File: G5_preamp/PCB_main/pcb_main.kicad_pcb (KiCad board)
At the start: 2 copper layers, 165 x 58 mm, 47 parts, among them J1 PSU_TUBE, J2 PCB_TUBE, J3 PSU_AMP, J4 AMP, J5 PSU_SIMCAB, J6 SIMCAB, J8 LEVEL 3-2, SW1 Boost, SW2 SIMCAB

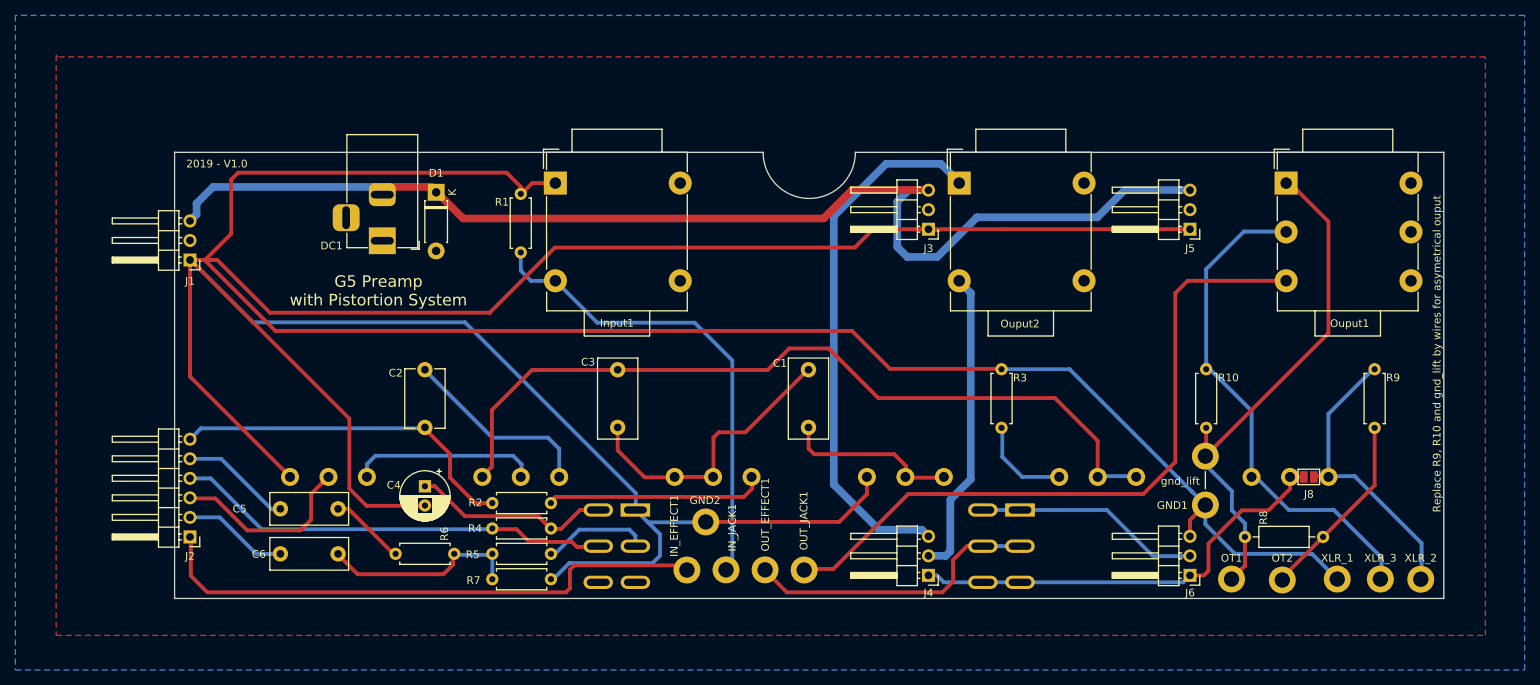
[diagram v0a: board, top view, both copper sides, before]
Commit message: DC-DC move
DC-DC Converter move from PCB_tube to PCB_main
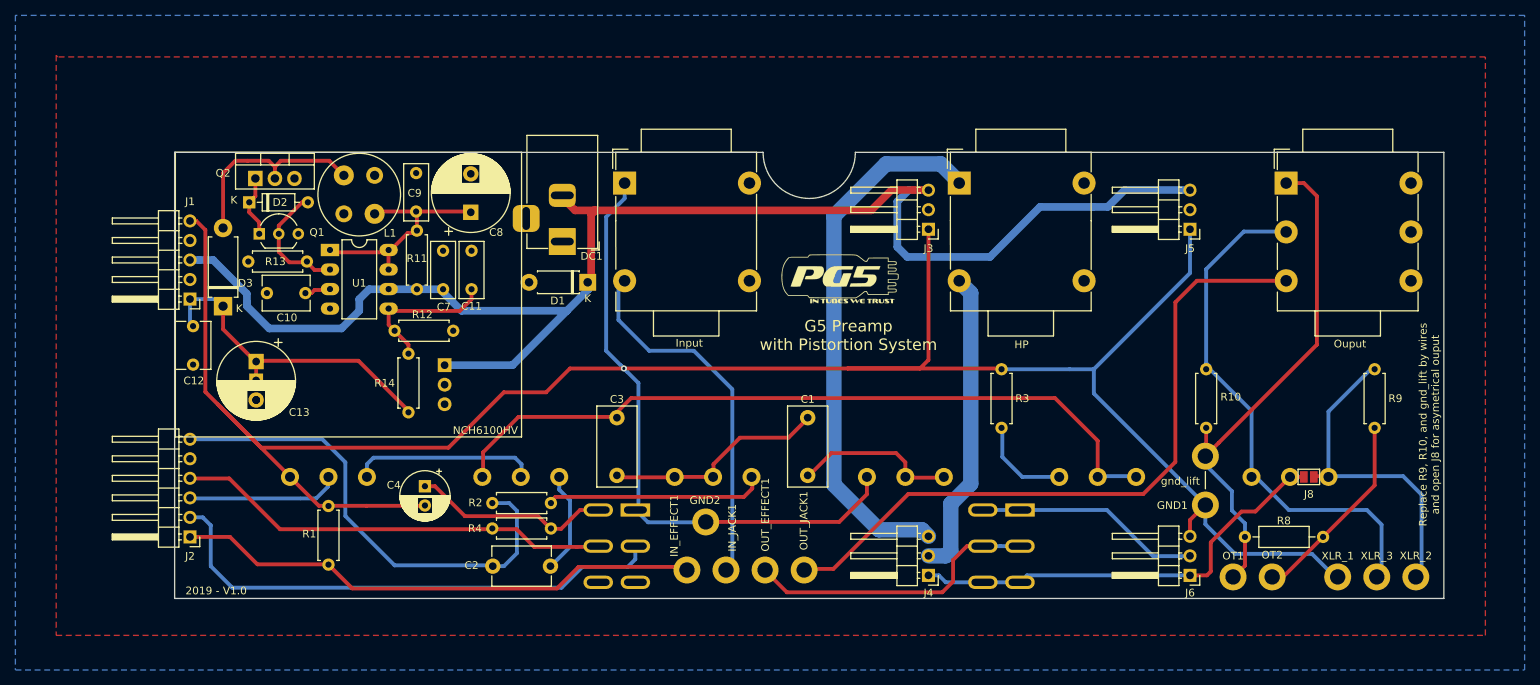
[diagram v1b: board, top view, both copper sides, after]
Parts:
- removed C5, C6: 22nF, Capacitor_THT:C_Rect_L10.0mm_W4.0mm_P7.50mm_MKS4
- removed Input1: Input, ProjectLib_main:Jack_6.35mm_Neutrik_NMJ4HCD2_Horizontal
- removed Ouput2: HP, ProjectLib_main:Jack_6.35mm_Neutrik_NMJ4HCD2_Horizontal
- removed R5: 100k, Resistor_THT:R_Axial_DIN0207_L6.3mm_D2.5mm_P7.62mm_Horizontal
- removed R6, R7: 470k, Resistor_THT:R_Axial_DIN0207_L6.3mm_D2.5mm_P7.62mm_Horizontal
- added C10: 470p, Capacitor_THT:C_Disc_D6.0mm_W4.4mm_P5.00mm, F.Cu at (97.0, 120.3)
- added C11: 100n, Capacitor_THT:C_Rect_L7.2mm_W3.0mm_P5.00mm_FKS2_FKP2_MKS2_MKP2, F.Cu at (118.6, 119.8)
- added C12: 10n/400V, Capacitor_THT:C_Disc_D6.0mm_W4.4mm_P5.00mm, F.Cu at (82.4, 124.6)
- added C13: 4.7µ/350V, Capacitor_THT:CP_Radial_D10.0mm_P5.00mm, F.Cu at (90.6, 129.2)
- added C7: 100n, Capacitor_THT:C_Rect_L7.2mm_W3.0mm_P5.00mm_FKS2_FKP2_MKS2_MKP2, F.Cu at (114.9, 119.8)
- added C8: 470µ, Capacitor_THT:CP_Radial_D10.0mm_P5.00mm, F.Cu at (118.5, 109.8)
- added C9: 100n, Capacitor_THT:C_Rect_L7.2mm_W3.0mm_P5.00mm_FKS2_FKP2_MKS2_MKP2, F.Cu at (111.4, 109.7)
- added D2: 1N4148, Diode_THT:D_DO-35_SOD27_P7.62mm_Horizontal, F.Cu at (89.7, 108.5)
- added D3: BYV26, Diode_THT:D_DO-15_P10.16mm_Horizontal, F.Cu at (86.3, 122.0)
- added HP: HP, ProjectLib_main:Jack_6.35mm_Neutrik_NMJ4HCD2_Horizontal, F.Cu at (182.0, 118.7)
- added Input: Input, ProjectLib_main:Jack_6.35mm_Neutrik_NMJ4HCD2_Horizontal, F.Cu at (138.5, 118.7)
- added L1: 220µH/1.5A, ProjectLib_main:L_Radial_D10.5mm_P5.00mm_MuRATA_1200RS, F.Cu at (106.0, 110.0)
- added NCH6100HV: NCH6100HV, Converter_DCDC:NCH6100HV, F.Cu at (125.1, 139.0)
- added Q1: MPS751, Package_TO_SOT_THT:TO-92_Inline_Wide, F.Cu at (91.0, 112.6)
- added Q2: IRF740, Package_TO_SOT_THT:TO-220-3_Vertical, F.Cu at (90.5, 105.4)
- added R11: 0.22R, Resistor_THT:R_Axial_DIN0207_L6.3mm_D2.5mm_P7.62mm_Horizontal, F.Cu at (111.5, 119.8)
- added R12: 1.8k, Resistor_THT:R_Axial_DIN0207_L6.3mm_D2.5mm_P7.62mm_Horizontal, F.Cu at (108.6, 125.2)
- added R13: 1k, Resistor_THT:R_Axial_DIN0207_L6.3mm_D2.5mm_P7.62mm_Horizontal, F.Cu at (97.2, 116.2)
- added R14: 430k, Resistor_THT:R_Axial_DIN0207_L6.3mm_D2.5mm_P7.62mm_Horizontal, F.Cu at (110.4, 135.8)
- added REF**: PG5_Logo_15mm_SilkScreen, Symbol:PG5_Logo_15mm_SilkScreen, F.Cu at (166.5, 118.2)
- added U1: MC34063AP, Package_DIP:DIP-8_W7.62mm_LongPads, F.Cu at (100.2, 114.7)
- J1: footprint Connector_PinHeader_2.54mm:PinHeader_1x03_P2.54mm_Horizontal -> Connector_PinHeader_2.54mm:PinHeader_1x05_P2.54mm_Horizontal
- SW1, SW2: footprint ProjectLib_main:SW_CK_Lever_DPDT_72xx -> Switch_lever:SW_CK_Lever_DPDT_72xx
- moved R1 47.7 mm to (100.0, 155.6)
- moved C2 30.3 mm to (128.9, 155.8), turned to 180 degrees
- moved DC1 23.4 mm to (130.4, 113.6)
- moved D1 22.9 mm to (133.7, 118.9), turned to 180 degrees
- moved C1 6.24 mm to (162.3, 136.5)
- moved C3 6.24 mm to (137.5, 136.5)
- moved J1 5.08 mm to (82.0, 121.1)
- moved OT2 1.38 mm to (222.7, 157.2)
- moved XLR_2 0.71 mm to (241.4, 157.2)
- moved XLR_3 0.55 mm to (236.3, 157.2)
- moved OT1 0.34 mm to (217.6, 157.2)
- moved XLR_1 0.29 mm to (231.2, 157.2)
- renumbered Ouput1 to Ouput
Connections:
- net /SIMCAB_IN renamed /LINE_OUT
- D1 pad 2: GND -> GNDREF
- DC1 pad 1: GND -> GNDREF
- J1 pad 1: GNDS -> /HT2
- J1 pad 2: GND -> Net-(J1-Pad2)
- J2 pad 2: /G_V2 -> /BOOST
- J2 pad 5: /A_V1B -> Net-(J2-Pad5)
- J3 pad 2: GND -> GNDREF
- J4 pad 2: Net-(J4-Pad2) -> /HP1
- J4 pad 3: Net-(J4-Pad3) -> /HP2
- J5 pad 2: GND -> GNDREF
- R1 pad 1: Net-(IN_JACK1-Pad1) -> /IN_EFFECT
- SW1 pad 2: Net-(R5-Pad2) -> /BOOST
- SW1 pad 3: (no net) -> Net-(SW1-Pad3)
- SW1 pad 6: (no net) -> Net-(SW1-Pad6)
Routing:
- net GNDS: track 580.3 -> 360.9 mm, vias 0 -> 1
- net Net-(J4-Pad3): track 70.0 -> 0.00 mm
- net /HP2: track 0.00 -> 70.0 mm
- net /BOOST: track 0.00 -> 68.0 mm
- net /HT2: track 0.00 -> 43.6 mm
- net /HP1: track 0.00 -> 39.9 mm
- net Net-(J4-Pad2): track 39.9 -> 0.00 mm
- net +24V: track 154.9 -> 194.4 mm
- net /PEAK: track 0.00 -> 29.7 mm
- net Net-(C6-Pad2): track 25.9 -> 0.00 mm
- net /HT1: track 0.00 -> 25.6 mm
- net Net-(C11-Pad1): track 0.00 -> 19.4 mm
- net /A_V1A: track 45.9 -> 63.2 mm
- net Net-(D2-Pad2): track 0.00 -> 16.2 mm
- net Net-(IN_JACK1-Pad1): track 62.5 -> 47.8 mm
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- added copper zone on B.Cu, net GNDREF
- added copper zone on F.Cu, net GNDREF
- removed copper zone on B.Cu, net GND
- removed copper zone on F.Cu, net GND
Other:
- board text added: "Replace R9, R10, and gnd_lift by wires and open J8 for asymetrical ouput"
- board text removed: "Replace R9, R10 and gnd_lift by wires for asymetrical ouput"

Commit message: Gerber export
Last MAJ with GERBER
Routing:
- net Net-(IN_JACK1-Pad1): track 47.8 -> 43.7 mm
- net GNDS: track 360.9 -> 362.4 mm
- net /G_V1B: track 19.8 -> 19.1 mm
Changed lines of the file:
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@@
     (thickness 1.6)
     (drawings 11)
-    (tracks 333)
+    (tracks 326)
     (zones 0)
     (modules 61)
@@
   (layers
     (0 F.Cu signal)
-    (31 B.Cu signal)
+    (31 B.Cu signal hide)
     (32 B.Adhes user)
     (33 F.Adhes user)
@@
     (visible_elements 7FFFFF7F)
     (pcbplotparams
-      (layerselection 0x010fc_ffffffff)
-      (usegerberextensions false)
+      (layerselection 0x010f0_ffffffff)
+      (usegerberextensions true)
       (usegerberattributes false)
       (usegerberadvancedattributes false)
@@
       (drillshape 0)
       (scaleselection 1)
-      (outputdirectory ""))
+      (outputdirectory "GERBER/"))
   )
   (net 0 "")
@@
   (gr_line (start 245 160) (end 245 102) (layer Edge.Cuts) (width 0.1))
   (gr_line (start 80 160) (end 245 160) (layer Edge.Cuts) (width 0.1))
-  (segment (start 212 106.9) (end 203.5 106.9) (width 1) (layer B.Cu) (net 1) (status 10))
   (segment (start 82 116) (end 81.9 116.1) (width 1) (layer F.Cu) (net 1) (status 30))
   (segment (start 82.1 116) (end 82.05 116) (width 1) (layer B.Cu) (net 1) (status 30))
@@
   (segment (start 134.449999 109.549999) (end 132.049999 109.549999) (width 1) (layer F.Cu) (net 1))
   (segment (start 132.049999 109.549999) (end 130.1 107.6) (width 1) (layer F.Cu) (net 1) (status 20))
-  (segment (start 201.3 109.1) (end 199.4 109.1) (width 1) (layer B.Cu) (net 1))
-  (segment (start 203.5 106.9) (end 201.3 109.1) (width 1) (layer B.Cu) (net 1))
-  (segment (start 175.45 106.9) (end 178.1 106.9) (width 1) (layer B.Cu) (net 1))
-  (segment (start 192.5 109.1) (end 186 115.6) (width 1) (layer B.Cu) (net 1))
-  (segment (start 199.4 109.1) (end 192.5 109.1) (width 1) (layer B.Cu) (net 1))
-  (segment (start 186 115.6) (end 175.25 115.6) (width 1) (layer B.Cu) (net 1))
-  (segment (start 175.25 115.6) (end 173.95 114.3) (width 1) (layer B.Cu) (net 1))
-  (segment (start 173.95 114.3) (end 173.95 108.4) (width 1) (layer B.Cu) (net 1))
-  (segment (start 173.95 108.4) (end 175.45 106.9) (width 1) (layer B.Cu) (net 1))
   (segment (start 89.4 121.5) (end 89.4 120.4) (width 1) (layer B.Cu) (net 1))
   (segment (start 92.3 124.9) (end 89.4 122) (width 1) (layer B.Cu) (net 1))
@@
   (segment (start 134.700001 109.549999) (end 134.153294 110.096706) (width 1) (layer F.Cu) (net 1))
   (segment (start 134.153294 110.096706) (end 134.153294 118.546706) (width 1) (layer F.Cu) (net 1))
+  (segment (start 175.45 106.9) (end 178.1 106.9) (width 1) (layer B.Cu) (net 1))
+  (segment (start 203.5 106.9) (end 195.2 115.2) (width 1) (layer B.Cu) (net 1))
+  (segment (start 195.2 115.2) (end 174.85 115.2) (width 1) (layer B.Cu) (net 1))
+  (segment (start 174.85 115.2) (end 173.95 114.3) (width 1) (layer B.Cu) (net 1))
+  (segment (start 173.95 114.3) (end 173.95 108.4) (width 1) (layer B.Cu) (net 1))
+  (segment (start 212 106.9) (end 203.5 106.9) (width 1) (layer B.Cu) (net 1))
+  (segment (start 173.95 108.4) (end 175.45 106.9) (width 1) (layer B.Cu) (net 1))
   (segment (start 175.2 144.3) (end 175.1 144.2) (width 0.5) (layer F.Cu) (net 2) (status 30))
   (segment (start 180 144.3) (end 175.2 144.3) (width 0.5) (layer F.Cu) (net 2) (status 30))
@@
   (segment (start 131.6 149.6) (end 132.7 148.5) (width 0.5) (layer F.Cu) (net 5))
   (segment (start 132.7 148.5) (end 135.4 148.5) (width 0.5) (layer F.Cu) (net 5))
-  (segment (start 127.25 149.3) (end 128.85 150.9) (width 0.5) (layer F.Cu) (net 5) (status 20))
-  (segment (start 117.734002 149.3) (end 127.25 149.3) (width 0.5) (layer F.Cu) (net 5))
-  (segment (start 112.4 145.41) (end 113.844002 145.41) (width 0.5) (layer F.Cu) (net 5) (status 10))
-  (segment (start 113.844002 145.41) (end 117.734002 149.3) (width 0.5) (layer F.Cu) (net 5))
-  (segment (start 137.7 119.5) (end 138.5 118.7) (width 0.5) (layer B.Cu) (net 6))
-  (segment (start 152.5 155.5) (end 152.5 132.8) (width 0.5) (layer B.Cu) (net 6))
+  (segment (start 127.242551 149.292551) (end 128.85 150.9) (width 0.5) (layer F.Cu) (net 5))
+  (segment (start 117.726553 149.292551) (end 127.242551 149.292551) (width 0.5) (layer F.Cu) (net 5))
+  (segment (start 112.4 145.41) (end 113.844002 145.41) (width 0.5) (layer F.Cu) (net 5))
+  (segment (start 113.844002 145.41) (end 117.726553 149.292551) (width 0.5) (layer F.Cu) (net 5))
+  (segment (start 138.5 118.8) (end 138.5 118.7) (width 0.5) (layer B.Cu) (net 6))
+  (segment (start 152.5 132.8) (end 138.5 118.8) (width 0.5) (layer B.Cu) (net 6))
   (segment (start 151.7 156.3) (end 152.5 155.5) (width 0.5) (layer B.Cu) (net 6))
-  (segment (start 152.5 132.8) (end 147.5 127.8) (width 0.5) (layer B.Cu) (net 6))
-  (segment (start 147.5 127.8) (end 141.7 127.8) (width 0.5) (layer B.Cu) (net 6))
-  (segment (start 141.7 127.8) (end 137.7 123.8) (width 0.5) (layer B.Cu) (net 6))
-  (segment (start 137.7 123.8) (end 137.7 119.5) (width 0.5) (layer B.Cu) (net 6))
+  (segment (start 152.5 155.5) (end 152.5 132.8) (width 0.5) (layer B.Cu) (net 6))
   (segment (start 161.763473 156.163473) (end 161.8 156.2) (width 0.5) (layer F.Cu) (net 7))
   (segment (start 212.9 118.7) (end 210.1 121.5) (width 0.5) (layer F.Cu) (net 7))
@@
   (segment (start 185.17 153.2) (end 182.995 153.2) (width 0.5) (layer F.Cu) (net 11) (status 10))
   (segment (start 182.995 153.2) (end 181.2 154.995) (width 0.5) (layer F.Cu) (net 11))
-  (segment (start 185.17 148.5) (end 190.2 148.5) (width 0.5) (layer B.Cu) (net 12) (status 30))
-  (segment (start 190.2 148.5) (end 201.2 148.5) (width 0.5) (layer B.Cu) (net 12) (status 10))
-  (segment (start 201.2 148.5) (end 207.2 154.5) (width 0.5) (layer B.Cu) (net 12))
-  (segment (start 207.2 154.5) (end 212 154.5) (width 0.5) (layer B.Cu) (net 12) (status 20))
+  (segment (start 199.2 154.5) (end 212 154.5) (width 0.5) (layer B.Cu) (net 12))
+  (segment (start 185.17 148.5) (end 193.2 148.5) (width 0.5) (layer B.Cu) (net 12))
+  (segment (start 193.2 148.5) (end 199.2 154.5) (width 0.5) (layer B.Cu) (net 12))
   (segment (start 104.9 144.2) (end 105 144.1) (width 0.5) (layer F.Cu) (net 13) (status 30))
   (segment (start 125.1 142.55) (end 125.1 143.2) (width 0.5) (layer B.Cu) (net 13))
@@
   (segment (start 96.3 147) (end 82.1 147) (width 0.5) (layer B.Cu) (net 17) (status 20))
   (segment (start 100 144.2) (end 99.95 144.2) (width 0.5) (layer F.Cu) (net 17) (status 30))
-  (segment (start 98.4 147) (end 96.4 147) (width 0.5) (layer B.Cu) (net 17))
-  (segment (start 99.95 144.2) (end 99.95 145.45) (width 0.5) (layer B.Cu) (net 17) (status 10))
-  (segment (start 99.95 145.45) (end 98.4 147) (width 0.5) (layer B.Cu) (net 17))
-  (segment (start 87.2 152) (end 82.1 152) (width 0.5) (layer F.Cu) (net 18))
+  (segment (start 97.2 147) (end 96.4 147) (width 0.5) (layer B.Cu) (net 17))
+  (segment (start 99.95 144.2) (end 99.95 144.25) (width 0.5) (layer B.Cu) (net 17))
+  (segment (start 99.95 144.25) (end 97.2 147) (width 0.5) (layer B.Cu) (net 17))
+  (segment (start 85.666947 155.566947) (end 82.1 152) (width 0.5) (layer F.Cu) (net 18))
   (segment (start 146.3 155.9) (end 132.5 155.9) (width 0.5) (layer F.Cu) (net 18))
-  (segment (start 90.766947 155.566947) (end 87.2 152) (width 0.5) (layer F.Cu) (net 18))
   (segment (start 146.7 156.3) (end 146.3 155.9) (width 0.5) (layer F.Cu) (net 18))
   (segment (start 132.5 155.9) (end 129.7 158.7) (width 0.5) (layer F.Cu) (net 18))
   (segment (start 129.7 158.7) (end 103.1 158.7) (width 0.5) (layer F.Cu) (net 18))
   (segment (start 103.1 158.7) (end 99.966947 155.566947) (width 0.5) (layer F.Cu) (net 18))
-  (segment (start 99.966947 155.566947) (end 90.766947 155.566947) (width 0.5) (layer F.Cu) (net 18))
+  (segment (start 99.966947 155.566947) (end 85.666947 155.566947) (width 0.5) (layer F.Cu) (net 18))
   (segment (start 82 144.38) (end 82.02 144.4) (width 0.5) (layer B.Cu) (net 19) (status 30))
   (segment (start 132.3 153.3) (end 135.2 153.3) (width 0.5) (layer F.Cu) (net 19))
@@
   (segment (start 149.1 150.1) (end 141.55 150.1) (width 0.5) (layer B.Cu) (net 21))
   (segment (start 140.15 148.7) (end 140 148.7) (width 0.5) (layer B.Cu) (net 21))
-  (segment (start 212 112) (end 212 117.7) (width 0.5) (layer B.Cu) (net 21))
-  (segment (start 212 117.7) (end 199.5 130.2) (width 0.5) (layer B.Cu) (net 21))
   (segment (start 196.35 130.2) (end 199.5 130.2) (width 0.5) (layer B.Cu) (net 21))
-  (segment (start 199.5 133.35) (end 214 147.85) (width 0.5) (layer B.Cu) (net 21))
-  (segment (start 199.5 130.2) (end 199.5 133.35) (width 0.5) (layer B.Cu) (net 21))
   (segment (start 187.45 130.2) (end 187.35 130.1) (width 0.5) (layer F.Cu) (net 21))
   (segment (start 187.35 130.1) (end 167.5 130.1) (width 0.5) (layer F.Cu) (net 21))
@@
   (segment (start 138.5 106) (end 138.5 108) (width 0.5) (layer B.Cu) (net 21))
   (segment (start 138.5 108) (end 136.1 110.4) (width 0.5) (layer B.Cu) (net 21))
+  (segment (start 207.7 130.2) (end 199.5 130.2) (width 0.5) (layer B.Cu) (net 21))
+  (segment (start 207.7 141.55) (end 214 147.85) (width 0.5) (layer B.Cu) (net 21))
+  (segment (start 207.7 130.2) (end 207.7 141.55) (width 0.5) (layer B.Cu) (net 21))
+  (segment (start 207.7 116.3) (end 207.7 130.2) (width 0.5) (layer B.Cu) (net 21))
+  (segment (start 212 112) (end 207.7 116.3) (width 0.5) (layer B.Cu) (net 21))
   (segment (start 229.9 144.1) (end 230 144.2) (width 0.5) (layer F.Cu) (net 22) (status 30))
   (segment (start 228.2 144.1) (end 229.9 144.1) (width 0.5) (layer F.Cu) (net 22) (status 30))
